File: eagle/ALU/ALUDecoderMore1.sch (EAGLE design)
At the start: 0 parts

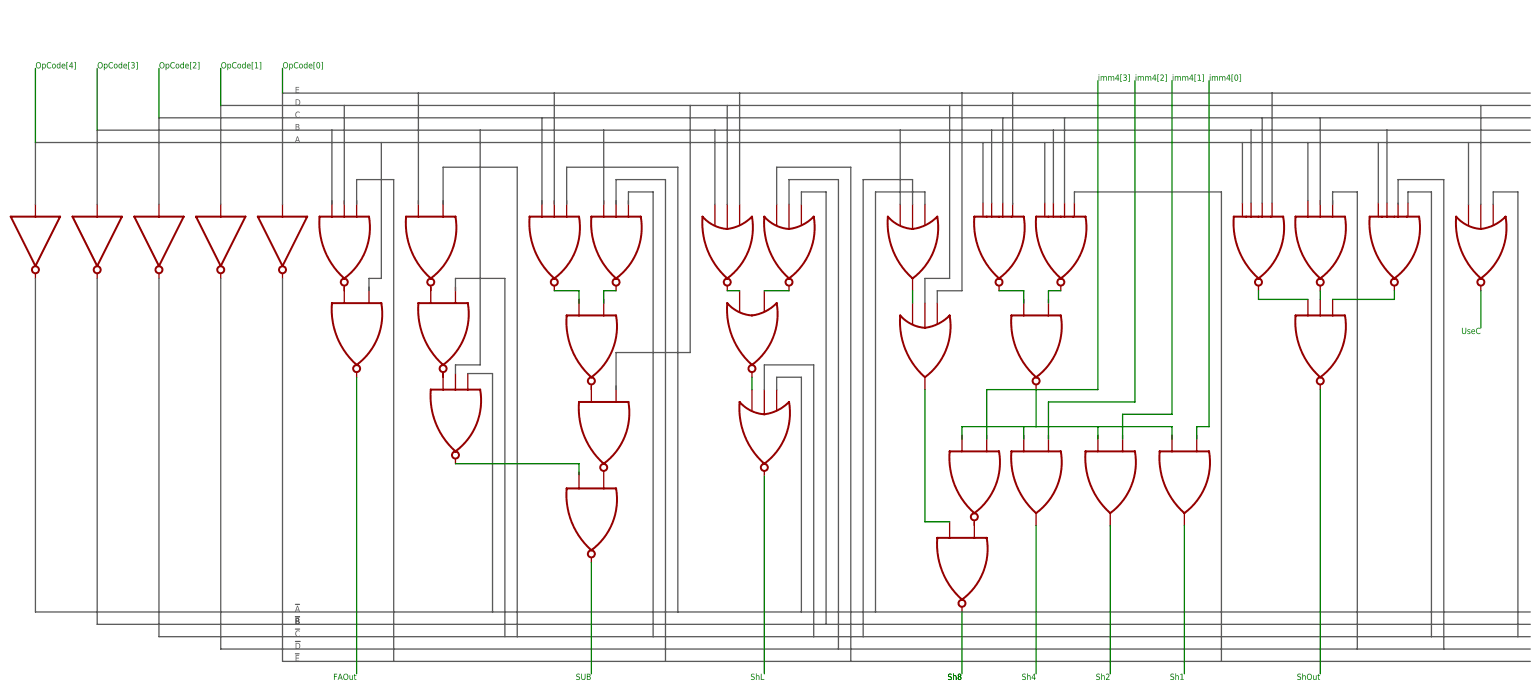
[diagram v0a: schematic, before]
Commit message: FR:ALU design reduction and rewording
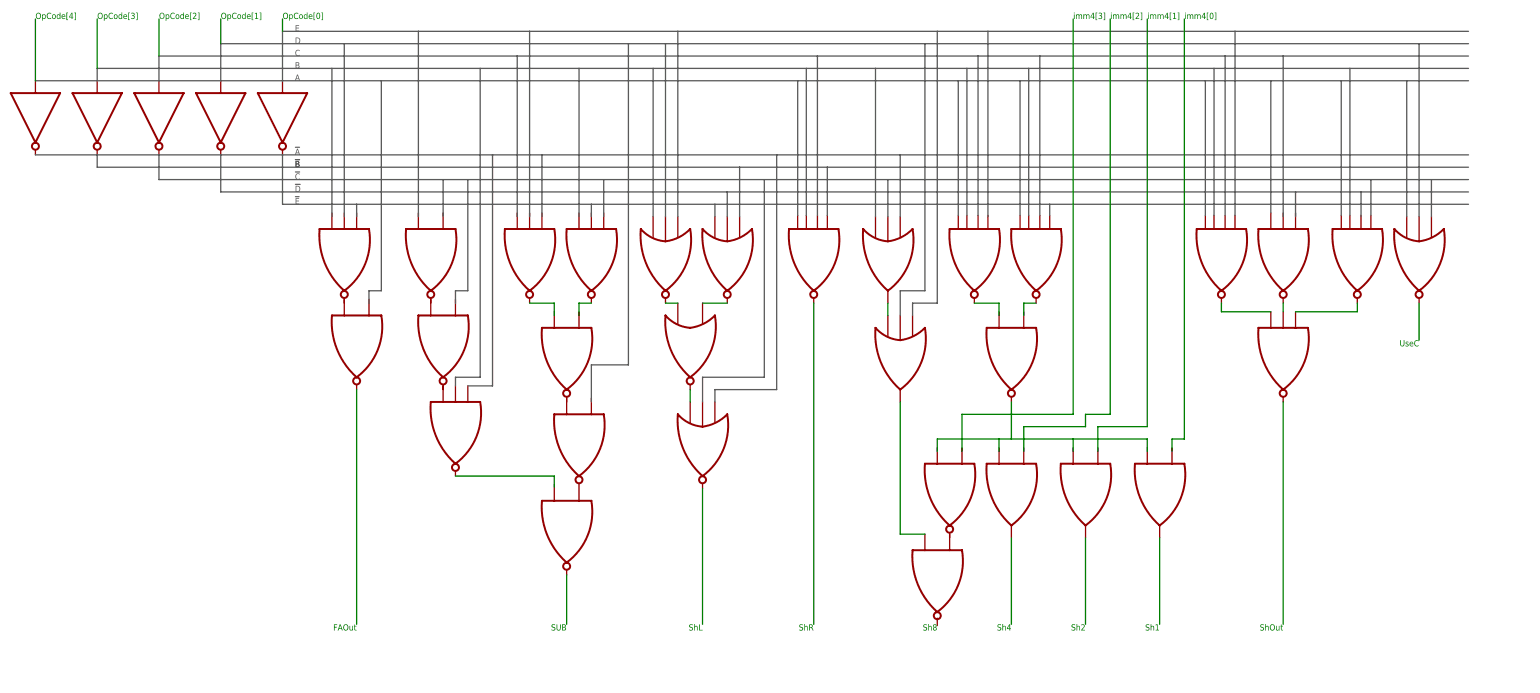
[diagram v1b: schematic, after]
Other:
- note added: "ShR"
